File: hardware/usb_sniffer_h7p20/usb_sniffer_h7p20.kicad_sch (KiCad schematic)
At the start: 75 parts, among them J4 USB_C_Receptacle_USB2.0_16P, J5 FFC-40P-0.5mm,NC, U1 H7P20N0L128-M3H1, U6 P25Q32SH-SSH-IT, U7 CY7C68013A-56LTX, U8 24C64BN, X1 XO32,26M,NC, Y2 24M

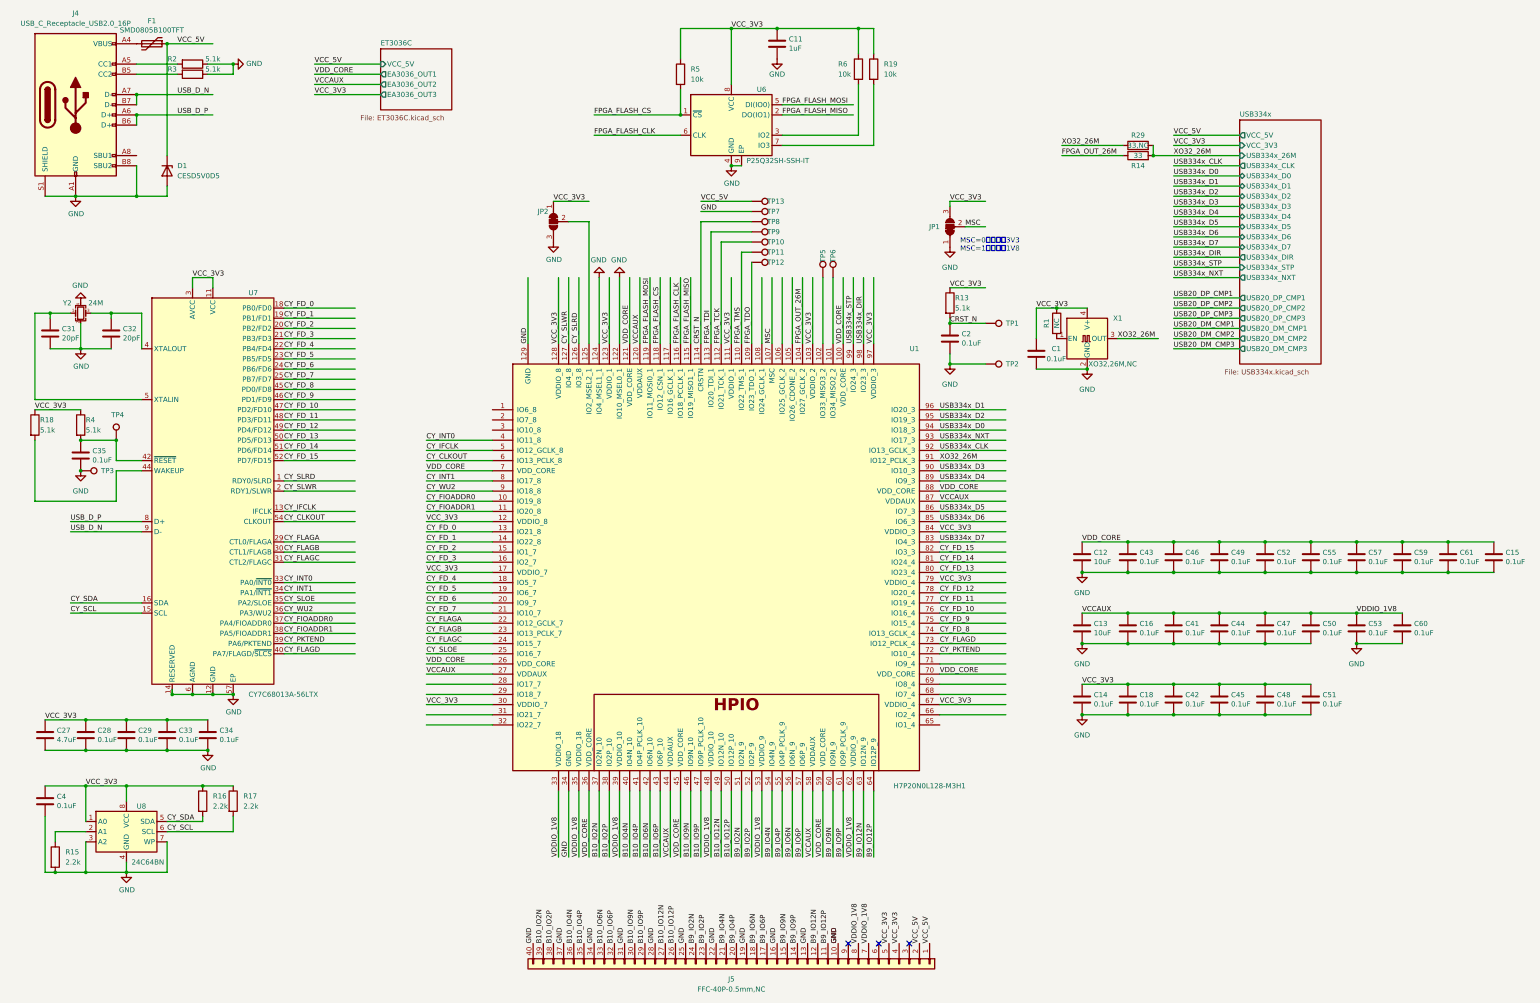
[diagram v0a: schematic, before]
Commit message: 增加辅助电路和优化焊盘工艺
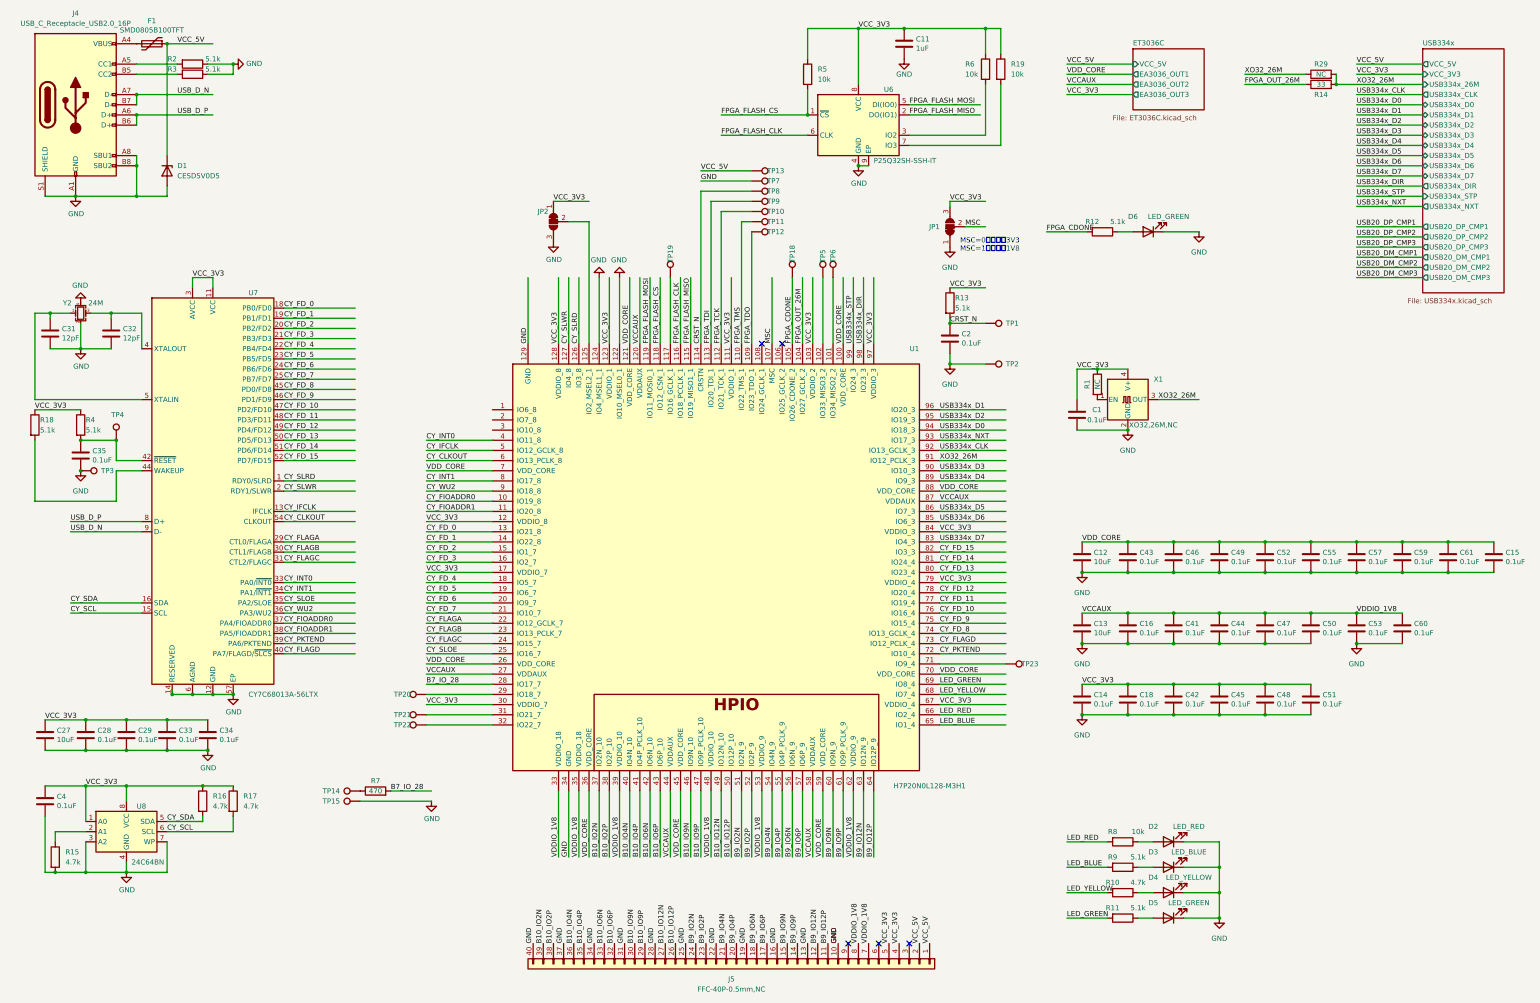
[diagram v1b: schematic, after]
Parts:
- added D2: LED_RED, LED_SMD:LED_0603_1608Metric, symbol Device:LED
- added D3: LED_BLUE, LED_SMD:LED_0603_1608Metric, symbol Device:LED
- added D4: LED_YELLOW, LED_SMD:LED_0603_1608Metric, symbol Device:LED
- added D5, D6: LED_GREEN, LED_SMD:LED_0603_1608Metric, symbol Device:LED
- added R10: 4.7k, Resistor_SMD:R_0402_1005Metric, symbol Device:R
- added R11, R12, R9: 5.1k, Resistor_SMD:R_0402_1005Metric, symbol Device:R
- added R7: 470, Resistor_SMD:R_0402_1005Metric, symbol Device:R
- added R8: 10k, Resistor_SMD:R_0402_1005Metric, symbol Device:R
- added TP14, TP15: TestPoint, vllogic:PinHeader_1x01_P1.00mm_Vertical, symbol Connector:TestPoint
- added TP18, TP19, TP20, TP21, TP22, TP23: TestPoint, vllogic:TestPoint_Pad_D0.3mm, symbol Connector:TestPoint
- C27: value 4.7uF -> 10uF
- C31, C32: value 20pF -> 12pF; footprint vllogic:C_0402_6mil -> Capacitor_SMD:C_0402_1005Metric
- R15, R16, R17: value 2.2k -> 4.7k
- R29: value 33,NC -> NC
- TP1, TP2, TP3, TP4: footprint (none) -> vllogic:PinHeader_1x01_P1.00mm_Vertical
- U7: footprint Package_DFN_QFN:QFN-56-1EP_8x8mm_P0.5mm_EP4.5x5.2mm_ThermalVias_TopTented -> Package_DFN_QFN:QFN-56-1EP_8x8mm_P0.5mm_EP4.5x5.2mm
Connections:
- net GND: now also J4.A8 (SBU1), D2.1 (K), D3.1 (K), D4.1 (K), D5.1 (K), D6.1 (K), TP15.1
- net FPGA_CDONE: now reaches U1.105 (IO26_CDONE_2)
- net FPGA_CDONE: now also R12.2, TP18.1
- net at U1.117 (IO16_GCLK_1): now also TP19.1
- net B7_IO_28: now reaches U1.28 (IO17_7)
- net B7_IO_28: now also R7.2
- net at U1.29 (IO18_7): now also TP20.1
- net at U1.31 (IO21_7): now also TP21.1
- net at U1.32 (IO22_7): now also TP22.1
- net LED_BLUE: now reaches U1.65 (IO1_4)
- net LED_BLUE: now also R9.2
- net LED_RED: now reaches U1.66 (IO2_4)
- net LED_RED: now also R8.2
- net LED_YELLOW: now reaches U1.68 (IO7_4)
- net LED_YELLOW: now also R10.2
- net LED_GREEN: now reaches U1.69 (IO8_4)
- net LED_GREEN: now also R11.2
- net at U1.71 (IO9_4): now also TP23.1
- new net: D2.2 (A), R8.1
- new net: D5.2 (A), R11.1
- new net: D6.2 (A), R12.1
- new net: D3.2 (A), R9.1
- new net: R7.1, TP14.1
- new net: D4.2 (A), R10.1
- no-connect marks 3 -> 5
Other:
- moved on the sheet: C1, C11, R1, R14, R19, R29, R5, R6, TP10, TP11, TP12, TP13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

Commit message: hardware\usb_sniffer_h7p20\production_files.2025605
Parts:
- removed D4: LED_YELLOW, LED_SMD:LED_0603_1608Metric, symbol Device:LED
- removed D5: LED_GREEN, LED_SMD:LED_0603_1608Metric, symbol Device:LED
- removed JP2: SolderJumper_3_Bridged12, Jumper:SolderJumper-3_P1.3mm_Bridged12_RoundedPad1.0x1.5mm_NumberLabels, symbol Jumper:SolderJumper_3_Bridged12
- removed R10: 4.7k, Resistor_SMD:R_0402_1005Metric, symbol Device:R
- removed R11: 5.1k, Resistor_SMD:R_0402_1005Metric, symbol Device:R
- removed TP23, TP5: TestPoint, vllogic:TestPoint_Pad_D0.3mm, symbol Connector:TestPoint
- added C19, C54, C56: NC, Capacitor_SMD:C_0402_1005Metric, symbol Device:C
- added C58: 0.1uF, Capacitor_SMD:C_0402_1005Metric, symbol Device:C
- added C62: 10uF, Capacitor_SMD:C_0402_1005Metric, symbol Device:C
- added JP2, JP3, JP4: SolderJumper_2_Open, Jumper:SolderJumper-2_P1.3mm_Open_RoundedPad1.0x1.5mm, symbol Jumper:SolderJumper_2_Open
- added R24: 10k,1%, Resistor_SMD:R_0402_1005Metric, symbol Device:R
- added TP16: TestPoint, vllogic:TestPoint_Pad_D0.3mm, symbol Connector:TestPoint
- added U9: CJ3439KDW, Package_TO_SOT_SMD:SOT-363_SC-70-6, symbol vllogic_chip:CJ3439KDW
- C2: value 0.1uF -> 1uF
- R12, R13, R18, R2, R3, R4, R9: value 5.1k -> 5.1k,1%
- R19, R5, R6, R8: value 10k -> 10k,1%
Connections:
- net LED_GREEN is gone; now on net USB20_DM_CMP2: U1.69 (IO8_4)
- net LED_YELLOW is gone; now on net USB20_DM_CMP1: U1.68 (IO7_4)
- net GND: now also C19.1, C54.1, C56.1, C58.1, C62.1, U9.1 (S1); no longer U1.122 (IO10_MSEL0_1), U1.124 (IO4_MSEL1_1)
- net USB20_DM_CMP3: now also U1.108 (IO24_GCLK_1)
- net USB20_DP_CMP1: now also U1.71 (IO9_4)
- net USB20_DP_CMP2: now also U1.102 (IO33_MISO3_2)
- net USB20_DP_CMP3: now also U1.106 (IO25_GCLK_2)
- net VCCAUX: now also R24.2, U9.4 (S2); no longer C47.2, C53.2, U1.33 (VDDIO_18), U1.35 (VDDIO_18), U1.39 (VDDIO_10), U1.48 (VDDIO_10), U1.53 (VDDIO_9), U1.62 (VDDIO_9)
- net VCC_3V3: now also JP2.2 (B), JP3.2 (B), JP4.2 (B), U9.2 (G1)
- net VDD_CORE: now also C19.2, C54.2, C56.2
- net FPGA_MSEL2: now reaches U1.125 (IO2_MSEL2_1)
- net FPGA_MSEL2: now also JP4.1 (A)
- net at U1.1 (IO6_8): now also TP16.1
- new net: R24.1, U9.5 (G2), U9.6 (D1)
- new net FPGA_MSEL0: JP2.1 (A), U1.122 (IO10_MSEL0_1)
- new net FPGA_MSEL1: JP3.1 (A), U1.124 (IO4_MSEL1_1)
- new net VDDIO_1V8: C47.2, C53.2, C58.2, C62.2, U1.33 (VDDIO_18), U1.35 (VDDIO_18), U1.39 (VDDIO_10), U1.48 (VDDIO_10), U1.53 (VDDIO_9), U1.62 (VDDIO_9), U9.3 (D2)
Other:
- note added: "CJ3439KDW原理示意图"
- note added: "上电顺序：VCC_5V --- 0R >>> OUT2(VCCAUX) --- 5.1k 1uF RC >>> OUT1(0.95V) --- 10k 1uF RC >>> OUT3(3.3V) CJ3439KDW在3.3V上电后，导通VCCAUX到VDDIO_1V8"
- moved on the sheet: C1, C12, C13, C14, C15, C16, C18, C41, C42, C43, C44, C45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

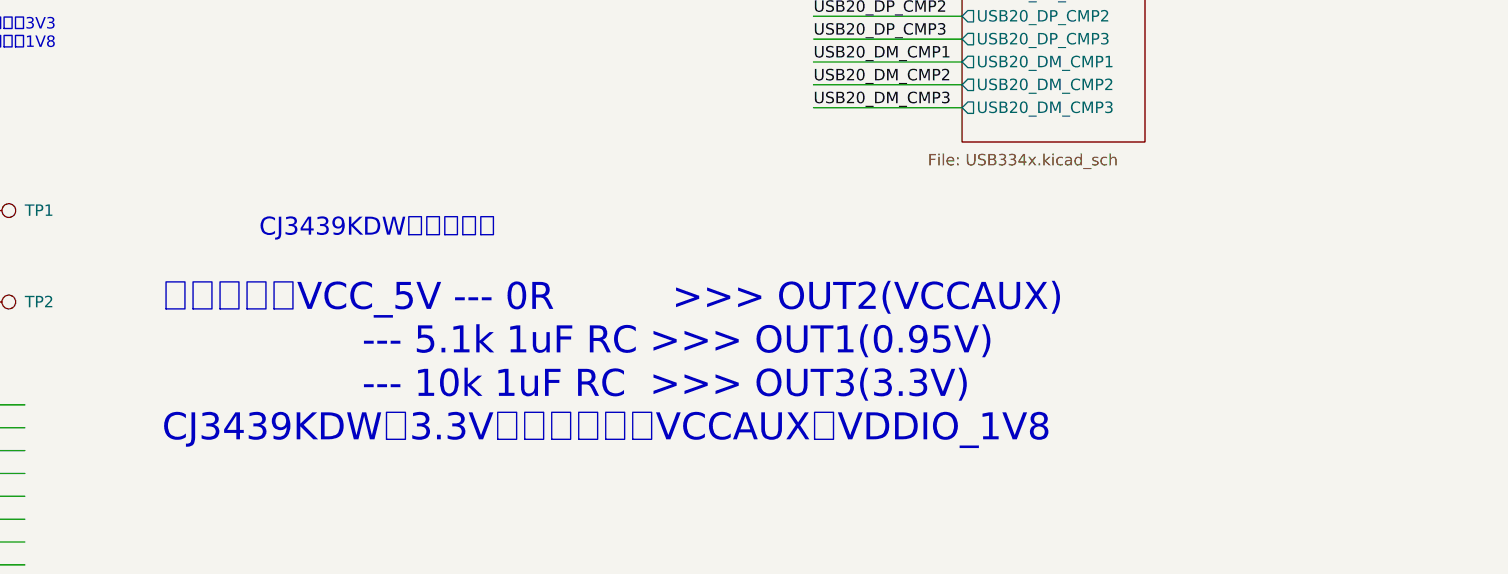
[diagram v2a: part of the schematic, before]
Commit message: 调整上电顺序为 5V -> core 0.95V -> vccaux 1.8V -> vccio
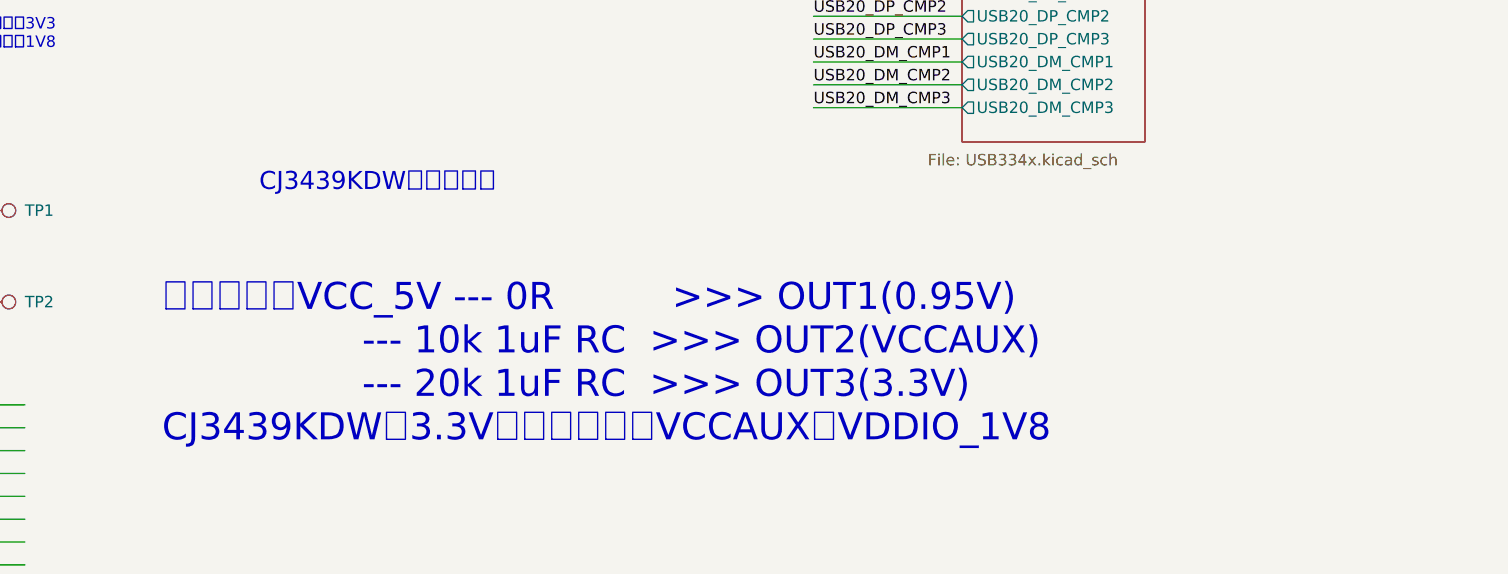
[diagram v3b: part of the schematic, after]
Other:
- note added: "上电顺序：VCC_5V --- 0R >>> OUT1(0.95V) --- 10k 1uF RC >>> OUT2(VCCAUX) --- 20k 1uF RC >>> OUT3(3.3V) CJ3439KDW在3.3V上电后，导通VCCAUX到VDDIO_1V8"
- note removed: "上电顺序：VCC_5V --- 0R >>> OUT2(VCCAUX) --- 5.1k 1uF RC >>> OUT1(0.95V) --- 10k 1uF RC >>> OUT3(3.3V) CJ3439KDW在3.3V上电后，导通VCCAUX到VDDIO_1V8"
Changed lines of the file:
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@@
     )
   )
-  (text "CJ3439KDW原理示意图" (at 288.925 94.615 0)
+  (text "CJ3439KDW原理示意图" (at 288.925 89.535 0)
     (effects (font (size 2 2)) (justify left bottom))
   )
@@
     (effects (font (size 1.27 1.27)) (justify left bottom))
   )
-  (text "上电顺序：VCC_5V --- 0R          >>> OUT2(VCCAUX)\n                 --- 5.1k 1uF RC >>> OUT1(0.95V)\n                 --- 10k 1uF RC  >>> OUT3(3.3V)\nCJ3439KDW在3.3V上电后，导通VCCAUX到VDDIO_1V8"
+  (text "上电顺序：VCC_5V --- 0R          >>> OUT1(0.95V)\n                 --- 10k 1uF RC  >>> OUT2(VCCAUX)\n                 --- 20k 1uF RC  >>> OUT3(3.3V)\nCJ3439KDW在3.3V上电后，导通VCCAUX到VDDIO_1V8"
     (at 278.13 117.475 0)
     (effects (font (size 3 3)) (justify left bottom))
